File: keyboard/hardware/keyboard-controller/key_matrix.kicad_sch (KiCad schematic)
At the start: 21 parts, among them J3 Keybed Connector, SW10 REST, SW3 OCTAVE_UP, SW4 OCTAVE_DOWN, SW5 PLAY_PAUSE, SW6 STOP, SW7 RECORD, SW8 HOLD, SW9 FUNC, U6 74HC164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

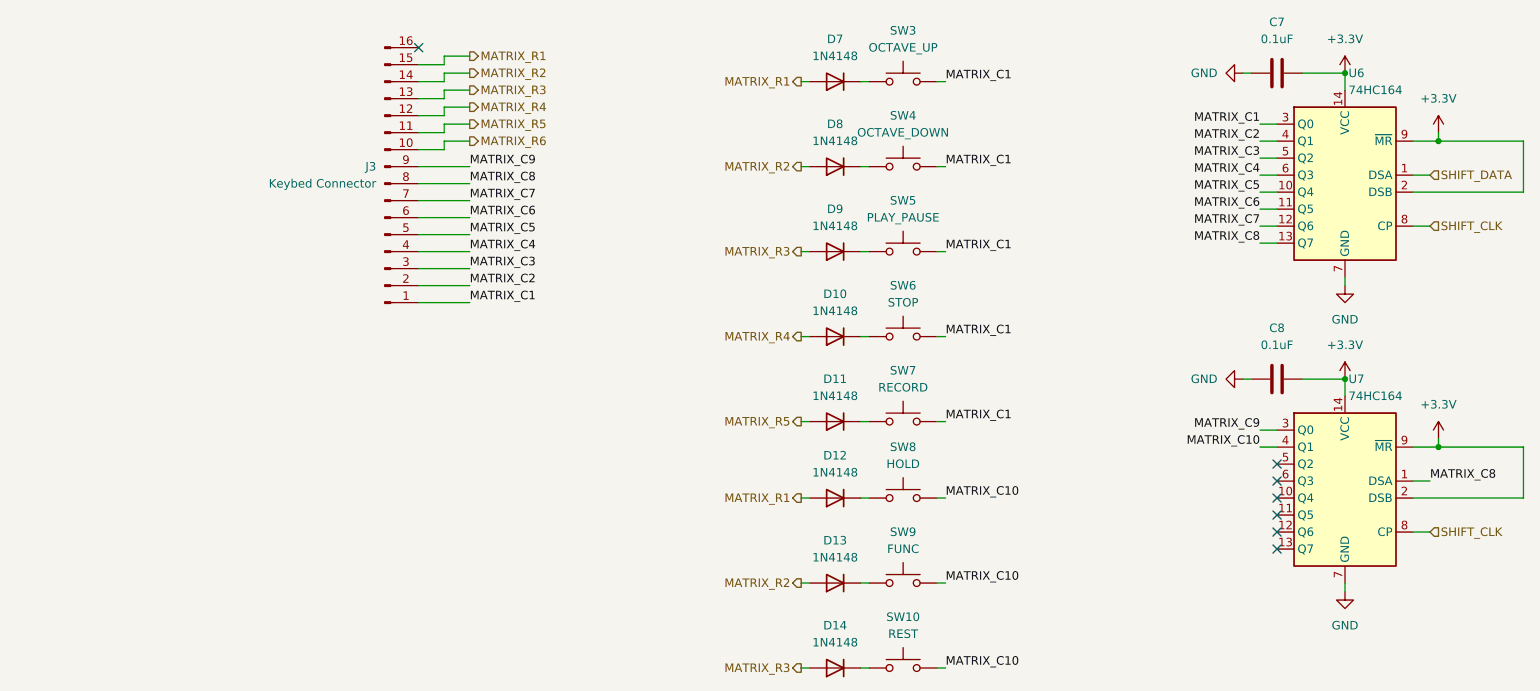
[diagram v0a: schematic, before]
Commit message: Simplified keyboard for rev1
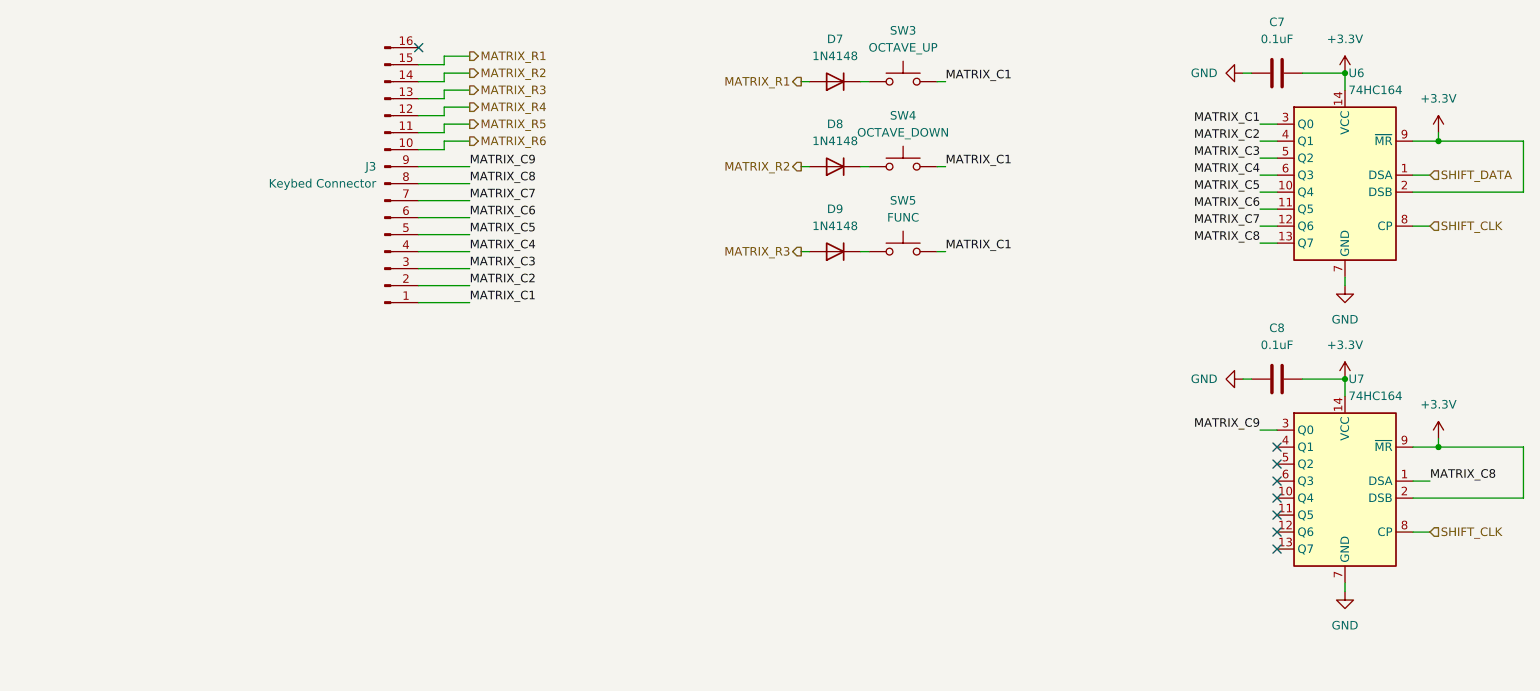
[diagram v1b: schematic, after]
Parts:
- removed D10, D11, D12, D13, D14: 1N4148, Diode_THT:D_DO-35_SOD27_P7.62mm_Horizontal, symbol Diode:1N4148
- removed SW10: REST, Button_Switch_THT:SW_PUSH_6mm, symbol Switch:SW_Push
- removed SW6: STOP, Button_Switch_THT:SW_PUSH_6mm, symbol Switch:SW_Push
- removed SW7: RECORD, Button_Switch_THT:SW_PUSH_6mm, symbol Switch:SW_Push
- removed SW8: HOLD, Button_Switch_THT:SW_PUSH_6mm, symbol Switch:SW_Push
- removed SW9: FUNC, Button_Switch_THT:SW_PUSH_6mm, symbol Switch:SW_Push
- SW5: value PLAY_PAUSE -> FUNC
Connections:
- net MATRIX_C10: no longer names the net of U7.4 (Q1)
- no-connect marks 7 -> 8

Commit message: Finalized keyboard controller rev1 board
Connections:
- net GND: now also J3.16 (Pin_16)
- no-connect marks 8 -> 7
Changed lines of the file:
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@@
   (no_connect (at 205.74 116.84))
   (no_connect (at 205.74 114.3))
-  (no_connect (at 77.47 46.99))
   (no_connect (at 205.74 119.38))
   (no_connect (at 205.74 111.76))
@@
     (stroke (width 0) (type default) (color 0 0 0 0))
   )
+  (wire (pts (xy 81.28 45.72) (xy 83.82 45.72))
+    (stroke (width 0) (type default) (color 0 0 0 0))
+  )
   (wire (pts (xy 226.06 66.04) (xy 228.6 66.04))
     (stroke (width 0) (type default) (color 0 0 0 0))
@@
     (stroke (width 0) (type default) (color 0 0 0 0))
   )
+  (wire (pts (xy 81.28 46.99) (xy 81.28 45.72))
+    (stroke (width 0) (type default) (color 0 0 0 0))
+  )
   (wire (pts (xy 77.47 80.01) (xy 85.09 80.01))
     (stroke (width 0) (type default) (color 0 0 0 0))
@@
   )
   (wire (pts (xy 134.62 52.07) (xy 135.89 52.07))
+    (stroke (width 0) (type default) (color 0 0 0 0))
+  )
+  (wire (pts (xy 77.47 46.99) (xy 81.28 46.99))
     (stroke (width 0) (type default) (color 0 0 0 0))
   )
@@
     (pin "2")
   )
+  (symbol (lib_id "power:GND") (at 83.82 45.72 90) (unit 1)
+    (in_bom yes) (on_board yes) (fields_autoplaced)
+    (property "Reference" "#PWR0101" (id 0) (at 90.17 45.72 0)
+      (effects (font (size 1.27 1.27)) hide)
+    )
+    (property "Value" "GND" (id 1) (at 87.63 45.7199 90)
+      (effects (font (size 1.27 1.27)) (justify right))
+    )
+    (property "Footprint" "" (id 2) (at 83.82 45.72 0)
+      (effects (font (size 1.27 1.27)) hide)
+    )
+    (property "Datasheet" "" (id 3) (at 83.82 45.72 0)
+      (effects (font (size 1.27 1.27)) hide)
+    )
+    (pin "1")
+  )
   (symbol (lib_id "Switch:SW_Push") (at 149.86 64.77 0) (unit 1)

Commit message: Fixes to keyboard controller rev1
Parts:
- SW3: value OCTAVE_UP -> FUNC
- SW4: value OCTAVE_DOWN -> OCTAVE_UP
- SW5: value FUNC -> OCTAVE_DOWN
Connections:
- net GND: no longer J3.16 (Pin_16)
- net MATRIX_C1: now also J3.16 (Pin_16); no longer J3.1 (Pin_1)
- net MATRIX_C2: now also J3.15 (Pin_15); no longer J3.2 (Pin_2)
- net MATRIX_C3: now also J3.14 (Pin_14); no longer J3.3 (Pin_3)
- net MATRIX_C4: now also J3.13 (Pin_13); no longer J3.4 (Pin_4)
- net MATRIX_C5: now also J3.12 (Pin_12); no longer J3.5 (Pin_5)
- net MATRIX_C6: now also J3.11 (Pin_11); no longer J3.6 (Pin_6)
- net MATRIX_C7: now also J3.10 (Pin_10); no longer J3.7 (Pin_7)
- net MATRIX_C8: now also J3.9 (Pin_9); no longer J3.8 (Pin_8)
- net MATRIX_C9: now also J3.8 (Pin_8); no longer J3.9 (Pin_9)
- net MATRIX_R1: now also J3.2 (Pin_2); no longer J3.15 (Pin_15)
- net MATRIX_R2: now also J3.3 (Pin_3); no longer J3.14 (Pin_14)
- net MATRIX_R3: now also J3.4 (Pin_4); no longer J3.13 (Pin_13)
- net MATRIX_R4: now also J3.5 (Pin_5); no longer J3.12 (Pin_12)
- net MATRIX_R5: now also J3.6 (Pin_6); no longer J3.11 (Pin_11)
- net MATRIX_R6: now also J3.7 (Pin_7); no longer J3.10 (Pin_10)
- no-connect marks 7 -> 8
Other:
- moved on the sheet: J3

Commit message: Completed keyboard controller rev2
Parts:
- renumbered D7 to D6, D8 to D7, D9 to D8, SW3 to SW2, SW4 to SW3, SW5 to SW4
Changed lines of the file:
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@@
   (symbol (lib_id "Switch:SW_Push") (at 149.86 52.07 0) (unit 1)
     (in_bom yes) (on_board yes) (fields_autoplaced)
-    (property "Reference" "SW3" (id 0) (at 149.86 44.45 0))
+    (property "Reference" "SW2" (id 0) (at 149.86 44.45 0))
     (property "Value" "FUNC" (id 1) (at 149.86 46.99 0))
     (property "Footprint" "Button_Switch_THT:SW_PUSH_6mm" (id 2) (at 149.86 46.99 0)
@@
   (symbol (lib_id "Diode:1N4148") (at 139.7 52.07 180) (unit 1)
     (in_bom yes) (on_board yes) (fields_autoplaced)
-    (property "Reference" "D7" (id 0) (at 139.7 45.72 0))
+    (property "Reference" "D6" (id 0) (at 139.7 45.72 0))
     (property "Value" "1N4148" (id 1) (at 139.7 48.26 0))
     (property "Footprint" "Diode_THT:D_DO-35_SOD27_P7.62mm_Horizontal" (id 2) (at 139.7 47.625 0)
@@
   (symbol (lib_id "Switch:SW_Push") (at 149.86 64.77 0) (unit 1)
     (in_bom yes) (on_board yes) (fields_autoplaced)
-    (property "Reference" "SW4" (id 0) (at 149.86 57.15 0))
+    (property "Reference" "SW3" (id 0) (at 149.86 57.15 0))
     (property "Value" "OCTAVE_UP" (id 1) (at 149.86 59.69 0))
     (property "Footprint" "Button_Switch_THT:SW_PUSH_6mm" (id 2) (at 149.86 59.69 0)
@@
   (symbol (lib_id "Diode:1N4148") (at 139.7 64.77 180) (unit 1)
     (in_bom yes) (on_board yes) (fields_autoplaced)
-    (property "Reference" "D8" (id 0) (at 139.7 58.42 0))
+    (property "Reference" "D7" (id 0) (at 139.7 58.42 0))
     (property "Value" "1N4148" (id 1) (at 139.7 60.96 0))
     (property "Footprint" "Diode_THT:D_DO-35_SOD27_P7.62mm_Horizontal" (id 2) (at 139.7 60.325 0)
@@
   (symbol (lib_id "power:GND") (at 215.9 82.55 0) (unit 1)
     (in_bom yes) (on_board yes) (fields_autoplaced)
-    (property "Reference" "#PWR039" (id 0) (at 215.9 88.9 0)
+    (property "Reference" "#PWR029" (id 0) (at 215.9 88.9 0)
       (effects (font (size 1.27 1.27)) hide)
     )
@@
   (symbol (lib_id "Switch:SW_Push") (at 149.86 77.47 0) (unit 1)
     (in_bom yes) (on_board yes) (fields_autoplaced)
-    (property "Reference" "SW5" (id 0) (at 149.86 69.85 0))
+    (property "Reference" "SW4" (id 0) (at 149.86 69.85 0))
     (property "Value" "OCTAVE_DOWN" (id 1) (at 149.86 72.39 0))
     (property "Footprint" "Button_Switch_THT:SW_PUSH_6mm" (id 2) (at 149.86 72.39 0)
@@
   (symbol (lib_id "power:GND") (at 200.66 50.8 270) (unit 1)
     (in_bom yes) (on_board yes) (fields_autoplaced)
-    (property "Reference" "#PWR036" (id 0) (at 194.31 50.8 0)
+    (property "Reference" "#PWR026" (id 0) (at 194.31 50.8 0)
       (effects (font (size 1.27 1.27)) hide)
     )
@@
   (symbol (lib_id "power:+3.3V") (at 229.87 105.41 0) (unit 1)
     (in_bom yes) (on_board yes) (fields_autoplaced)
-    (property "Reference" "#PWR043" (id 0) (at 229.87 109.22 0)
+    (property "Reference" "#PWR033" (id 0) (at 229.87 109.22 0)
       (effects (font (size 1.27 1.27)) hide)
     )
@@
   (symbol (lib_id "power:GND") (at 200.66 96.52 270) (unit 1)
     (in_bom yes) (on_board yes) (fields_autoplaced)
-    (property "Reference" "#PWR037" (id 0) (at 194.31 96.52 0)
+    (property "Reference" "#PWR027" (id 0) (at 194.31 96.52 0)
       (effects (font (size 1.27 1.27)) hide)
     )
@@
   (symbol (lib_id "Diode:1N4148") (at 139.7 77.47 180) (unit 1)
     (in_bom yes) (on_board yes) (fields_autoplaced)
-    (property "Reference" "D9" (id 0) (at 139.7 71.12 0))
+    (property "Reference" "D8" (id 0) (at 139.7 71.12 0))
     (property "Value" "1N4148" (id 1) (at 139.7 73.66 0))
     (property "Footprint" "Diode_THT:D_DO-35_SOD27_P7.62mm_Horizontal" (id 2) (at 139.7 73.025 0)
@@
   (symbol (lib_id "power:+3.3V") (at 215.9 96.52 0) (unit 1)
     (in_bom yes) (on_board yes) (fields_autoplaced)
-    (property "Reference" "#PWR040" (id 0) (at 215.9 100.33 0)
+    (property "Reference" "#PWR030" (id 0) (at 215.9 100.33 0)
       (effects (font (size 1.27 1.27)) hide)
     )
@@
   (symbol (lib_id "power:+3.3V") (at 229.87 59.69 0) (unit 1)
     (in_bom yes) (on_board yes) (fields_autoplaced)
-    (property "Reference" "#PWR042" (id 0) (at 229.87 63.5 0)
+    (property "Reference" "#PWR032" (id 0) (at 229.87 63.5 0)
       (effects (font (size 1.27 1.27)) hide)
     )
@@
   (symbol (lib_id "power:+3.3V") (at 215.9 50.8 0) (unit 1)
     (in_bom yes) (on_board yes) (fields_autoplaced)
-    (property "Reference" "#PWR038" (id 0) (at 215.9 54.61 0)
+    (property "Reference" "#PWR028" (id 0) (at 215.9 54.61 0)
       (effects (font (size 1.27 1.27)) hide)
     )
@@
   (symbol (lib_id "power:GND") (at 215.9 128.27 0) (unit 1)
     (in_bom yes) (on_board yes) (fields_autoplaced)
-    (property "Reference" "#PWR041" (id 0) (at 215.9 134.62 0)
-      (effects (font (size 1.27 1.27)) hide)
-    )
+    (property "Reference" "#PWR031" (id 0) (at 215.9 134.62 0)
+      (effects (font (size 1.27 1.27)) hide)
+    )
